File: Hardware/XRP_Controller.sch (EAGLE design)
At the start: 72 parts, among them J1 POWER_JACKPOWER_JACK_SLOT, J12 Vertical Qwiic Connector, J13 Vertical Qwiic Connector, J14 Vertical Qwiic Connector, J3 JST_6_PIN_VERTICAL, J4 JST_6_PIN_VERTICAL, J5 JST_6_PIN_VERTICAL, J6 JST_6_PIN_VERTICAL, J9 Vertical Qwiic Connector, M12_MODE JUMPER-SMT_2_NC_TRACE_SILK, M34_MODE JUMPER-SMT_2_NC_TRACE_SILK, Q3 20V/4.2A/52mΩ/1.4W, Q4 20V/4.2A/52mΩ/1.4W, Q5 20V/4.2A/52mΩ/1.4W, Q6 20V/4.2A/52mΩ/1.4W, U1 RPI_PICO_W, U2 AP63357, U4 LSM6DS0, U5 DRV8835, U6 DRV8835

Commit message: Clean up schematic
Add dashed lines between regions
Add I2C address for IMU
Add max voltages for motor drivers, 5V regulator, and Pico W
Rename jumpers and indicate functions
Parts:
- removed JP1, JP3: JUMPER-SMT_2_NO_SILK, SparkFun-Jumpers:JUMPER-SMT_2_NO_SILK
- removed JP2: JUMPER-SMT_3_2-NC_TRACE_SILK, SparkFun-Jumpers:JUMPER-SMT_3_2-NC_TRACE_SILK
- removed M12_MODE, M34_MODE: JUMPER-SMT_2_NC_TRACE_SILK, SparkFun-Jumpers:JUMPER-SMT_2_NC_TRACE_SILK
- added I2C: JUMPER-SMT_3_2-NC_TRACE_SILK, SparkFun-Jumpers:JUMPER-SMT_3_2-NC_TRACE_SILK
- added IMU_ADR, USB_POW: JUMPER-SMT_2_NO_SILK, SparkFun-Jumpers:JUMPER-SMT_2_NO_SILK
- added MOT_MODE_L, MOT_MODE_R: JUMPER-SMT_2_NC_TRACE_SILK, SparkFun-Jumpers:JUMPER-SMT_2_NC_TRACE_SILK
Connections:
- net 3.3V: now also I2C.2, MOT_MODE_L.2, MOT_MODE_R.2; no longer JP2.2, M12_MODE.2, M34_MODE.2
- net GND: now also IMU_ADR.1; no longer JP1.1
- net N$12: now also USB_POW.2; no longer JP3.2
- net N$13: now also MOT_MODE_L.1; no longer M12_MODE.1
- net N$14: now also MOT_MODE_R.1; no longer M34_MODE.1
- net N$2: now also IMU_ADR.2; no longer JP1.2
- net N$3: now also I2C.3; no longer JP2.3
- net N$4: now also I2C.1; no longer JP2.1
- net V_USB: now also USB_POW.1; no longer JP3.1
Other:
- note added: "32V max!"
- note added: "Close USB_POW jumper to power entire board from USB. WARNING!!! Do this at your own risk! Do not exceed the power limitations of your USB supply"
- note added: "Cut I2C jumper to remove pullup resistors"
- note added: "Cut MOT_MODE_L/R jumpers to change from PH/EN mode to PWM mode"
- note added: "Cut PWR jumper to remove power LED"
- note added: "Default I2C address: 0x6B Close IMU_ADR jumper: 0x6A"
- note added: "I2C Pullups"
- note added: "RPi Pico W"
- note added: "Reset Button"
- note added: "V_USB: 5.5V max!"
- note removed: "Buttons"
- note removed: "RP2040"
- moved on the sheet: C1, C10, C11, C12, C13, C2, C3, C4, C5, C6, C7, C8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

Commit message: Design review updates
Replace 2 power switch FETs with 1 at output of perfect diodes
Add perfect diode to make Pico's VSYS be input only
Extend board length to 2.125in
Move reset button away from edge, to center of left side
Swap right side motor IO pins
Rename connectors and corresponding nets
Change connector label silk to match
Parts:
- added Q7: (no value), SparkFun-DiscreteSemi:TRANS_PNP_DUALSOT-363
- added R7: 100k, SparkFun-Resistors:100KOHM-0603-1/10W-1%
- LOGO2: value QWIIC_LOGO_4MM -> QWIIC_LOGO_5MM; device SparkFun-Aesthetics:QWIIC_LOGO_4MM -> SparkFun-Aesthetics:QWIIC_LOGO_5MM
- R14: value 100k -> 1M; device SparkFun-Resistors:100KOHM-0603-1/10W-1% -> SparkFun-Resistors:1MOHM-0603-1/4W-5%
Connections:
- net MOT1_N renamed MOT_3_N
- net MOT1_P renamed MOT_3_P
- net MOT2_N renamed MOT_L_N
- net MOT2_P renamed MOT_L_P
- net MOT3_N renamed MOT_R_N
- net MOT3_P renamed MOT_R_P
- net MOT4_N renamed MOT_4_N
- net MOT4_P renamed MOT_4_P
- net RP_IO0/ENC1_A renamed RP_IO0/ENC_3_A
- net RP_IO1/ENC1_B renamed RP_IO1/ENC_3_B
- net RP_IO2/M1_PH renamed RP_IO2/MOT_3_PH
- net RP_IO3/M1_EN renamed RP_IO3/MOT_3_EN
- net RP_IO4/ENC2_A renamed RP_IO4/ENC_L_A
- net RP_IO5/ENC2_B renamed RP_IO5/ENC_L_B
- net RP_IO6/M2_PH renamed RP_IO6/MOT_L_PH
- net RP_IO7/M2_EN renamed RP_IO7/MOT_L_EN
- removed net RP_IO10/M3_PH: U1.GPIO10, U6.BIN1/PH
- removed net RP_IO11/M3_EN: U1.GPIO11, U6.BIN2/EN
- removed net RP_IO12/ENC4_A: J6.4, U1.GPIO12
- removed net RP_IO13/ENC4_B: J6.5, U1.GPIO13
- removed net RP_IO14/M4_PH: U1.GPIO14, U6.AIN1/PH
- removed net RP_IO15/M4_EN: U1.GPIO15, U6.AIN2/EN
- removed net RP_IO8/ENC3_A: J5.4, U1.GPIO8
- removed net RP_IO9/ENC3_B: J5.5, U1.GPIO9
- new net N$19: Q7G1.B, Q7G1.C, Q7G2.B, R7.2
- new net N$20: Q5.G, Q7G2.C, R14.2
- new net RP_IO10/MOT_4_PH: U1.GPIO10, U6.AIN1/PH
- new net RP_IO11/MOT_4_EN: U1.GPIO11, U6.AIN2/EN
- new net RP_IO12/ENC_R_A: J5.4, U1.GPIO12
- new net RP_IO13/ENC_R_B: J5.5, U1.GPIO13
- new net RP_IO14/MOT_R_PH: U1.GPIO14, U6.BIN1/PH
- new net RP_IO15/MOT_R_EN: U1.GPIO15, U6.BIN2/EN
- new net RP_IO8/ENC_4_A: J6.4, U1.GPIO8
- new net RP_IO9/ENC_4_B: J6.5, U1.GPIO9
- net !EN!: no longer Q5.G, R14.1
- net 5V: now also Q5.D, Q7G1.E; no longer U1.VSYS
- net GND: now also R14.1, R7.1
- net N$12: now also Q7G2.E, U1.VSYS; no longer R13.2, USB_POW.2
- net N$15: now also R13.2; no longer R14.2
- net N$17: now also Q6.S, R12.2; no longer F1.1
- net N$8: now also F1.1; no longer Q1G1.E, Q3.D
- net N$9: now also USB_POW.2; no longer Q5.D
- net RP_IO22: now also J13.3; no longer J13.4
- net RP_IO28: now also J13.4; no longer J13.3
- net V_BATT: now also Q1G1.E, Q3.D; no longer Q6.S, R12.2
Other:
- note added: "Expansion Connectors"
- note removed: "Qwiic Connector"
- moved on the sheet: F1, J1, Q1G1, Q1G2, Q2G1, Q2G2, Q3, Q4, Q5, Q6, R10, R11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

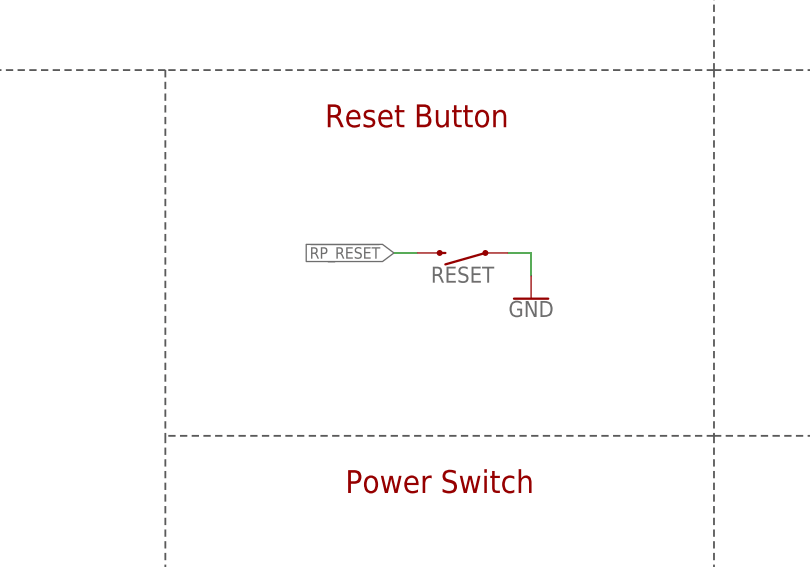
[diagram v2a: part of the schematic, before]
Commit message: Design review updates
Add debounce capacitor to reset button
Increase power trace widths to 25 mils
Pull 5V polygon out from under inductor and add GND vias
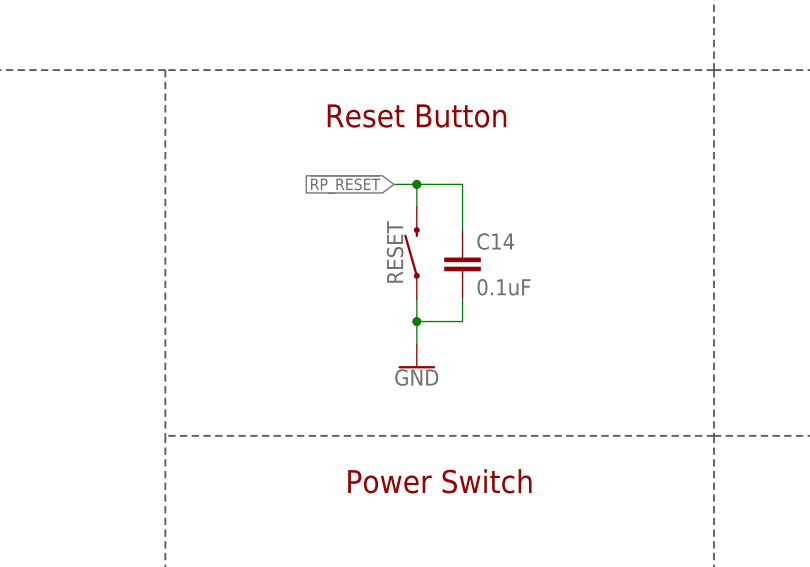
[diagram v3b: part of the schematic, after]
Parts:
- added C14: 0.1uF, SparkFun-Capacitors:0.1UF-0603-25V-(+80/-20%)
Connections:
- net !RP_RESET!: now also C14.1
- net GND: now also C14.2
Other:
- moved on the sheet: RESET
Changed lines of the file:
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@@
 <part name="GND28" library="SparkFun-PowerSymbols" deviceset="GND" device=""/>
 <part name="Q7" library="SparkFun-DiscreteSemi" deviceset="TRANS_PNP_DUAL" device="SOT-363" package3d_urn="urn:adsk.eagle:package:29757/2"/>
+<part name="C14" library="SparkFun-Capacitors" deviceset="0.1UF" device="-0603-25V-(+80/-20%)" value="0.1uF"/>
 </parts>
 <sheets>
@@
 <instance part="H3" gate="G$1" x="426.72" y="27.94" smashed="yes"/>
 <instance part="H4" gate="G$1" x="426.72" y="25.4" smashed="yes"/>
-<instance part="RESET" gate="G$1" x="213.36" y="83.82" smashed="yes" rot="R180">
-<attribute name="NAME" x="213.36" y="82.296" size="1.778" layer="95" font="vector" rot="R180" align="bottom-center"/>
-</instance>
-<instance part="GND10" gate="1" x="220.98" y="78.74" smashed="yes">
-<attribute name="VALUE" x="220.98" y="78.486" size="1.778" layer="96" font="vector" align="top-center"/>
+<instance part="RESET" gate="G$1" x="208.28" y="83.82" smashed="yes" rot="R90">
+<attribute name="NAME" x="206.756" y="83.82" size="1.778" layer="95" font="vector" rot="R90" align="bottom-center"/>
+</instance>
+<instance part="GND10" gate="1" x="208.28" y="71.12" smashed="yes">
+<attribute name="VALUE" x="208.28" y="70.866" size="1.778" layer="96" font="vector" align="top-center"/>
 </instance>
 <instance part="D1" gate="G$1" x="152.4" y="71.12" smashed="yes">
@@
 <attribute name="NAME" x="38.1" y="96.52" size="1.778" layer="95" font="vector"/>
 <attribute name="VALUE" x="38.1" y="96.266" size="1.778" layer="96" font="vector" align="top-left"/>
+</instance>
+<instance part="C14" gate="G$1" x="213.36" y="81.28" smashed="yes">
+<attribute name="NAME" x="214.884" y="84.201" size="1.778" layer="95" font="vector"/>
+<attribute name="VALUE" x="214.884" y="79.121" size="1.778" layer="96" font="vector"/>
 </instance>
 </instances>
@@
 <pinref part="GND10" gate="1" pin="GND"/>
 <pinref part="RESET" gate="G$1" pin="1"/>
-<wire x1="218.44" y1="83.82" x2="220.98" y2="83.82" width="0.1524" layer="91"/>
-<wire x1="220.98" y1="83.82" x2="220.98" y2="81.28" width="0.1524" layer="91"/>
+<wire x1="208.28" y1="78.74" x2="208.28" y2="76.2" width="0.1524" layer="91"/>
+<pinref part="C14" gate="G$1" pin="2"/>
+<wire x1="208.28" y1="76.2" x2="208.28" y2="73.66" width="0.1524" layer="91"/>
+<wire x1="213.36" y1="78.74" x2="213.36" y2="76.2" width="0.1524" layer="91"/>
+<wire x1="213.36" y1="76.2" x2="208.28" y2="76.2" width="0.1524" layer="91"/>
+<junction x="208.28" y="76.2"/>
 </segment>
 <segment>
@@
 <segment>
 <pinref part="RESET" gate="G$1" pin="2"/>
-<wire x1="208.28" y1="83.82" x2="205.74" y2="83.82" width="0.1524" layer="91"/>
-<label x="205.74" y="83.82" size="1.27" layer="95" font="vector" rot="R180" xref="yes"/>
-</segment>
-<segment>
+<label x="205.74" y="91.44" size="1.27" layer="95" font="vector" rot="R180" xref="yes"/>
+<pinref part="C14" gate="G$1" pin="1"/>
+<wire x1="205.74" y1="91.44" x2="208.28" y2="91.44" width="0.1524" layer="91"/>
+<wire x1="208.28" y1="91.44" x2="213.36" y2="91.44" width="0.1524" layer="91"/>
+<wire x1="213.36" y1="91.44" x2="213.36" y2="86.36" width="0.1524" layer="91"/>
+<wire x1="208.28" y1="88.9" x2="208.28" y2="91.44" width="0.1524" layer="91"/>
+<junction x="208.28" y="91.44"/>
+</segment>
+<segment>

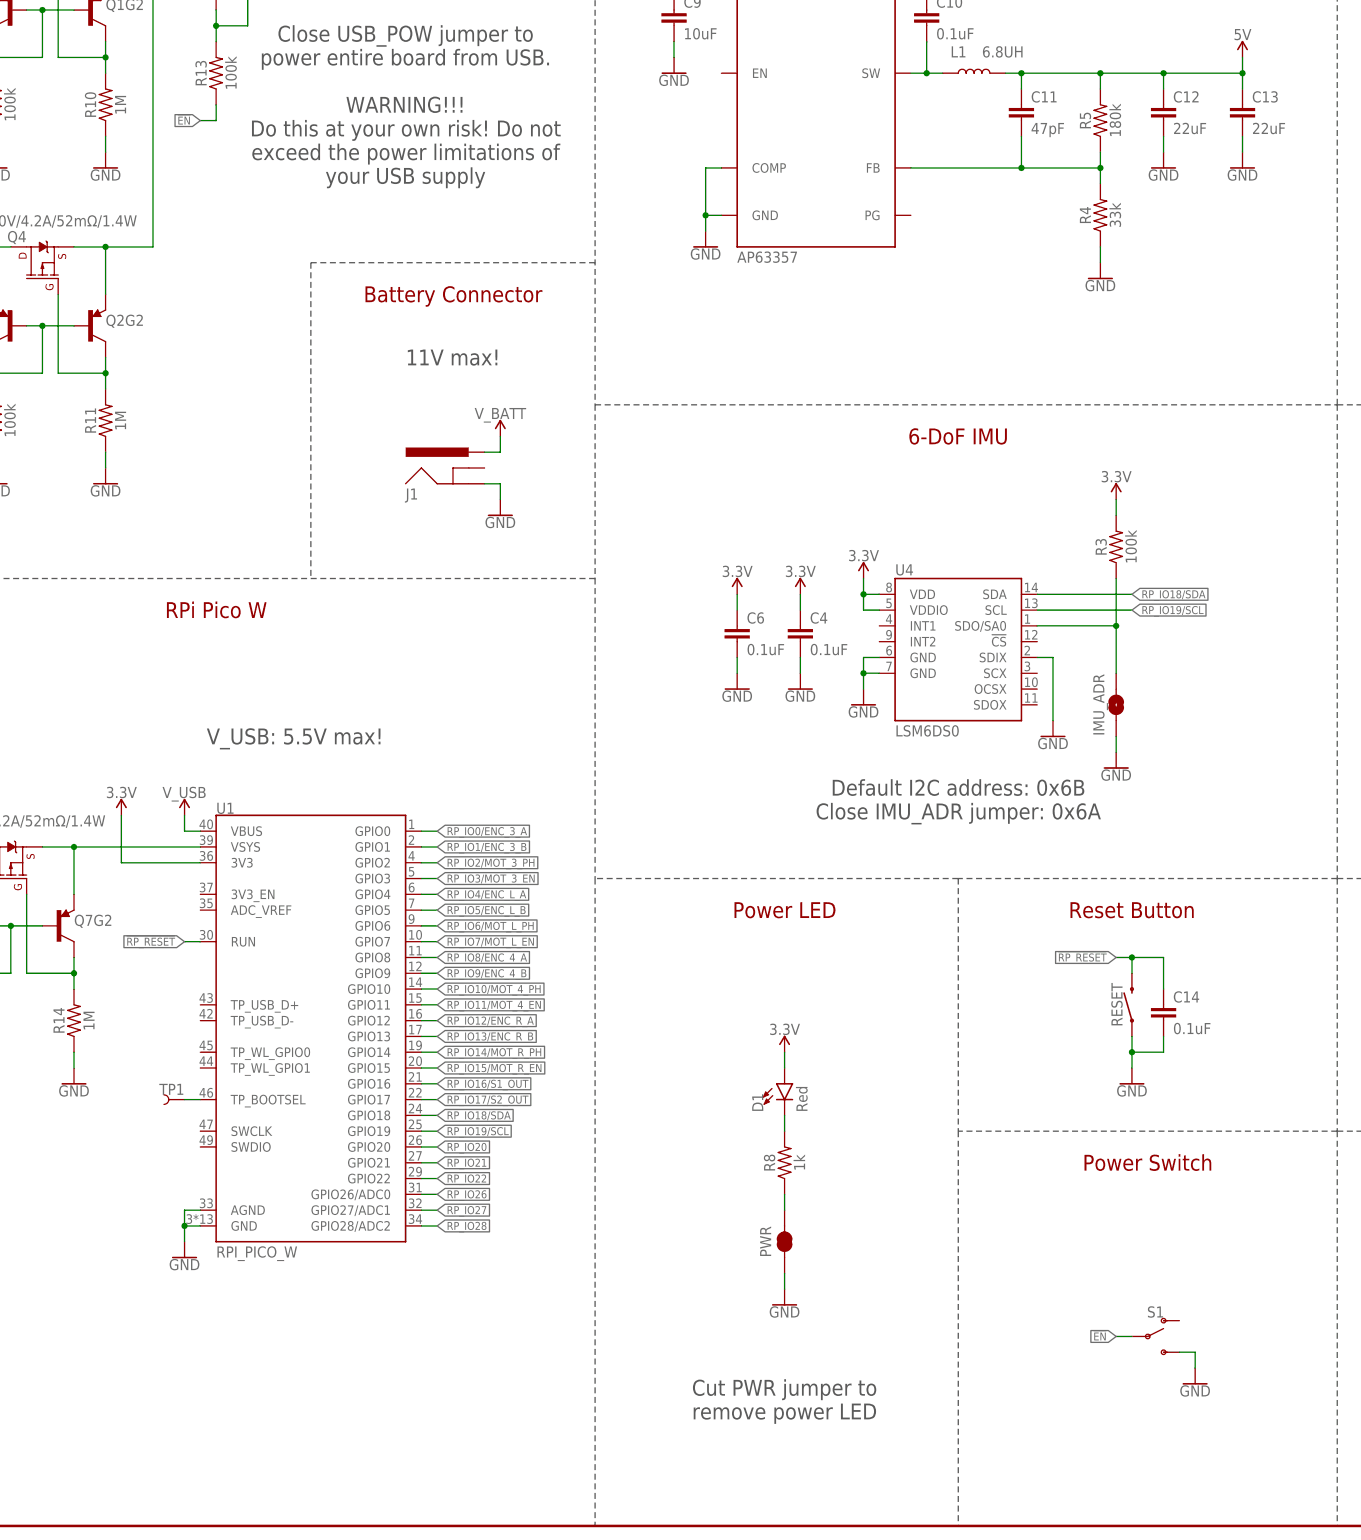
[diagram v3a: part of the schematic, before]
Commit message: Design review updates
Add silk lines between adjacent passive components
Rename "!EN!" net to "!POW_EN!"
Add text next to power switch indicating function
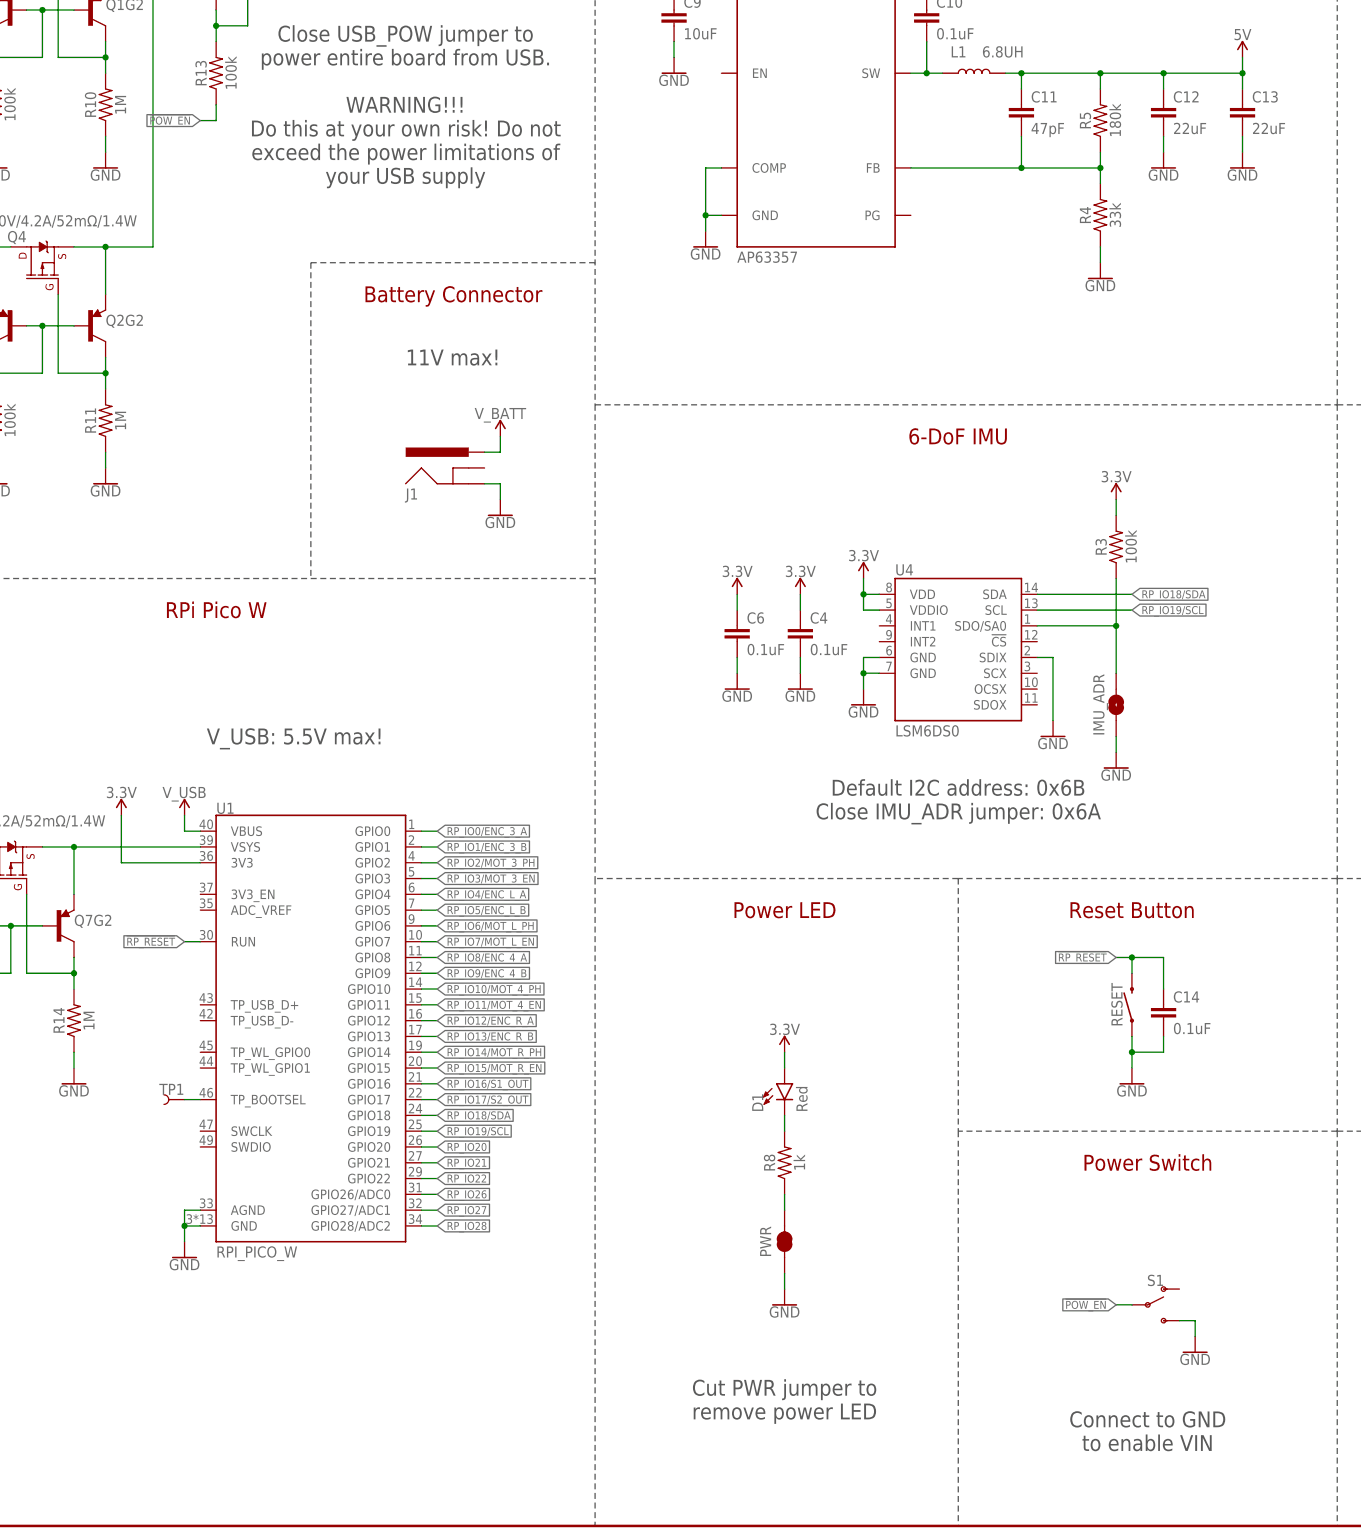
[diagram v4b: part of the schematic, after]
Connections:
- net !EN! renamed !POW_EN!
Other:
- note added: "Connect to GND to enable VIN"
- moved on the sheet: S1
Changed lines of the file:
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@@
 <text x="157.48" y="261.62" size="2.54" layer="97" font="vector" align="center">32V max!</text>
 <text x="327.66" y="266.7" size="2.54" layer="97" font="vector" align="center">11V max!</text>
+<text x="210.82" y="15.24" size="2.54" layer="97" font="vector" align="center">Connect to GND
+to enable VIN</text>
 </plain>
 <instances>
@@
 <attribute name="NAME" x="71.12" y="259.08" size="1.778" layer="95" font="vector" rot="MR180"/>
 </instance>
-<instance part="GND26" gate="1" x="218.44" y="22.86" smashed="yes">
-<attribute name="VALUE" x="218.44" y="22.606" size="1.778" layer="96" font="vector" align="top-center"/>
+<instance part="GND26" gate="1" x="218.44" y="27.94" smashed="yes">
+<attribute name="VALUE" x="218.44" y="27.686" size="1.778" layer="96" font="vector" align="top-center"/>
 </instance>
 <instance part="SUPPLY4" gate="G$1" x="91.44" y="259.08" smashed="yes">
@@
 <attribute name="VALUE" x="10.16" y="211.074" size="1.778" layer="96" font="vector" align="bottom-center"/>
 </instance>
-<instance part="S1" gate="1" x="210.82" y="30.48" smashed="yes">
-<attribute name="NAME" x="212.09" y="33.528" size="1.778" layer="95" font="vector" align="bottom-center"/>
-<attribute name="VALUE" x="211.836" y="27.178" size="1.778" layer="96" font="vector" align="top-center"/>
+<instance part="S1" gate="1" x="210.82" y="35.56" smashed="yes">
+<attribute name="NAME" x="212.09" y="38.608" size="1.778" layer="95" font="vector" align="bottom-center"/>
+<attribute name="VALUE" x="211.836" y="32.258" size="1.778" layer="96" font="vector" align="top-center"/>
 </instance>
 <instance part="SUPPLY6" gate="G$1" x="264.16" y="213.36" smashed="yes">
@@
 <segment>
 <pinref part="GND26" gate="1" pin="GND"/>
-<wire x1="218.44" y1="25.4" x2="218.44" y2="27.94" width="0.1524" layer="91"/>
-<wire x1="218.44" y1="27.94" x2="215.9" y2="27.94" width="0.1524" layer="91"/>
+<wire x1="218.44" y1="30.48" x2="218.44" y2="33.02" width="0.1524" layer="91"/>
+<wire x1="218.44" y1="33.02" x2="215.9" y2="33.02" width="0.1524" layer="91"/>
 <pinref part="S1" gate="1" pin="S"/>
 </segment>
@@
 </segment>
 </net>
-<net name="!EN!" class="0">
+<net name="!POW_EN!" class="0">
 <segment>
 <wire x1="60.96" y1="228.6" x2="60.96" y2="226.06" width="0.1524" layer="91"/>
@@
 </segment>
 <segment>
-<wire x1="208.28" y1="30.48" x2="205.74" y2="30.48" width="0.1524" layer="91"/>
-<label x="205.74" y="30.48" size="1.27" layer="95" font="vector" rot="R180" xref="yes"/>
+<wire x1="208.28" y1="35.56" x2="205.74" y2="35.56" width="0.1524" layer="91"/>
+<label x="205.74" y="35.56" size="1.27" layer="95" font="vector" rot="R180" xref="yes"/>
 <pinref part="S1" gate="1" pin="P"/>
 </segment>
